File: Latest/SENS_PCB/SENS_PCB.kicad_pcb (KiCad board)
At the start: 2 copper layers, 15 x 15 mm, 2 parts, among them J1 Conn_01x04_Female, U1 MS5840-02BA

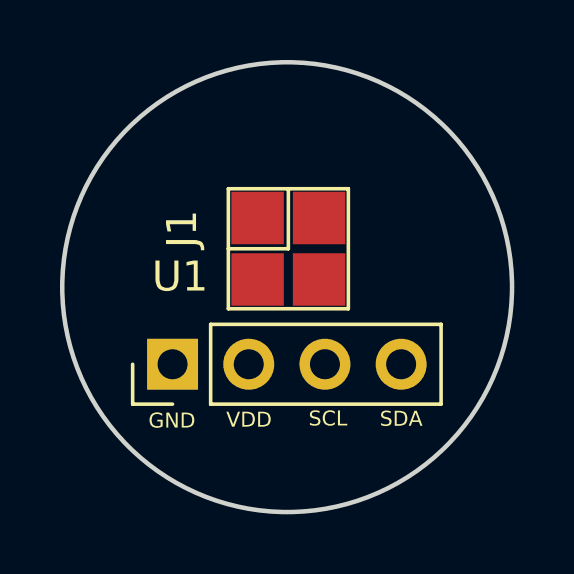
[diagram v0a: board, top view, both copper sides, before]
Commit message: Added pad connections
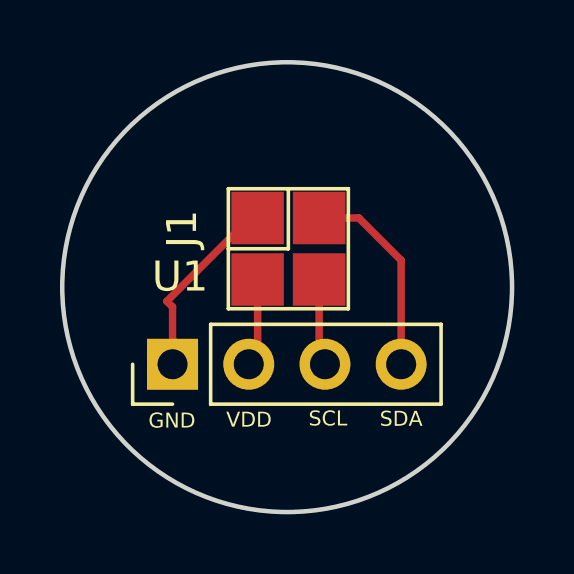
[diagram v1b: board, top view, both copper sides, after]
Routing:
- net Net-(J1-Pad4): track 0.00 -> 6.78 mm
- net Net-(J1-Pad1): track 0.00 -> 6.35 mm
- net Net-(J1-Pad2): track 0.00 -> 2.95 mm
- net Net-(J1-Pad3): track 0.00 -> 2.91 mm
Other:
- net class Default removed
